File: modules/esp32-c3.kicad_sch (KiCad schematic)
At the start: 20 parts, among them U2 ESP32-C3, U3 W25X40CLSN, Y1 40MHz

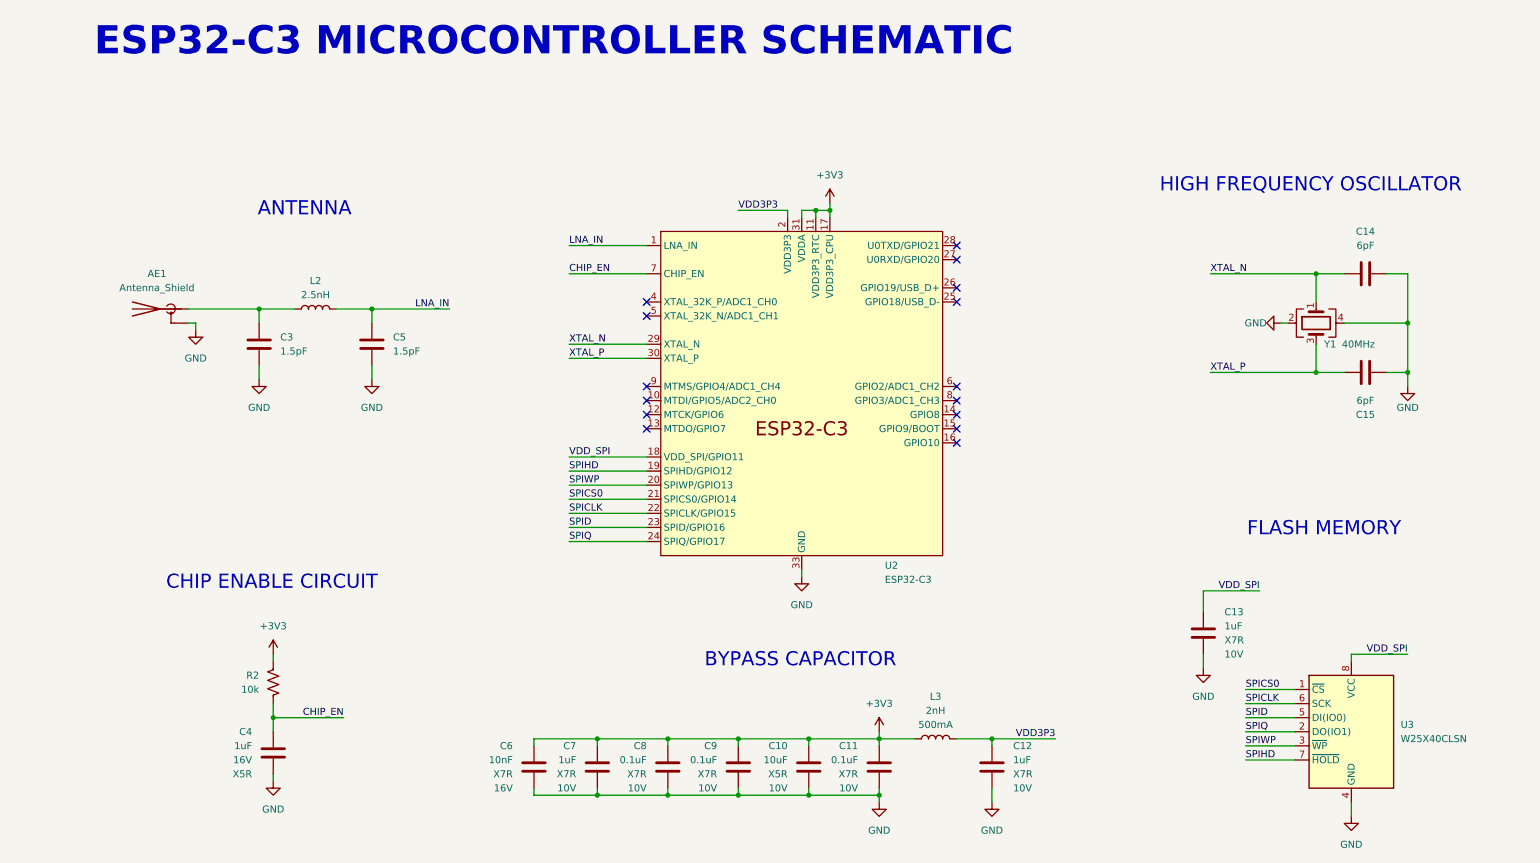
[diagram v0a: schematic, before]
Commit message: Made the first version of the layout with the ESP32-C3
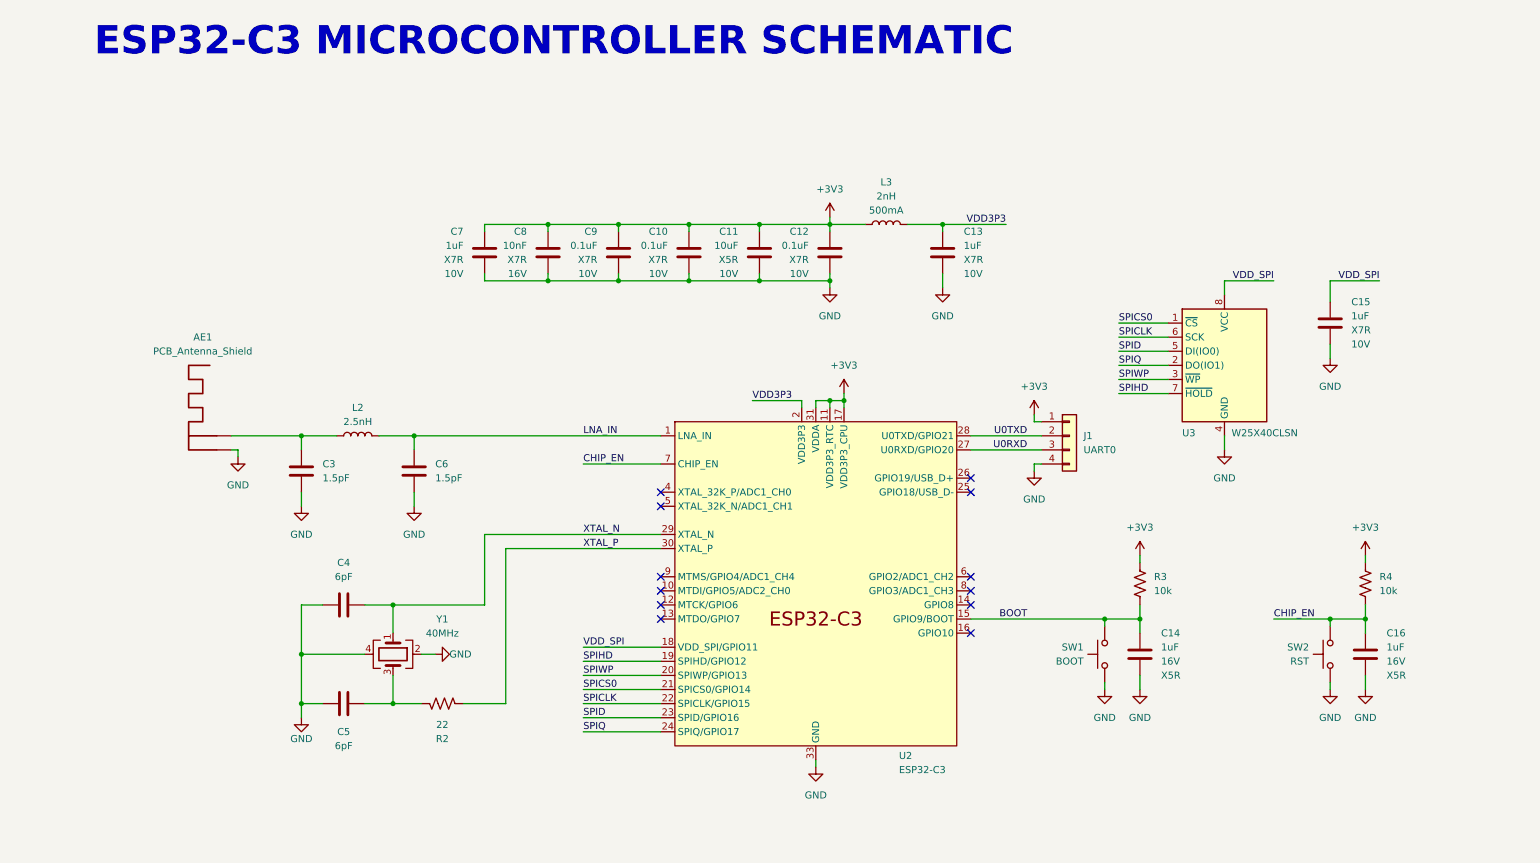
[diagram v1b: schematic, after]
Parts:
- removed AE1: Antenna_Shield, symbol Device:Antenna_Shield
- added AE1: PCB_Antenna_Shield, RF_Antenna:PCB_ANTENNA_2,4GHz_50Ohm, symbol Device:PCB_Antenna_Shield
- added C14: 1uF, Capacitor_SMD:C_0603_1608Metric, symbol Device:C
- added J1: UART0, Connector_PinHeader_2.00mm:PinHeader_1x04_P2.00mm_Vertical, symbol Connector_Generic:Conn_01x04
- added R2: 22, Resistor_SMD:R_0603_1608Metric, symbol Device:R_US
- added R3: 10k, Resistor_SMD:R_0603_1608Metric, symbol Device:R_US
- added SW1: BOOT, Button_Switch_THT:SW_PUSH_1P1T_6x3.5mm_H5.0_APEM_MJTP1250, symbol Switch:SW_Push
- added SW2: RST, Button_Switch_THT:SW_PUSH_1P1T_6x3.5mm_H5.0_APEM_MJTP1250, symbol Switch:SW_Push
- renumbered C9 to C10, C10 to C11, C11 to C12, C12 to C13, C13 to C15, C4 to C16, C14 to C4, C15 to C5, C5 to C6, C6 to C8, C8 to C9, R2 to R4
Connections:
- net +3V3: now also J1.1 (Pin_1), R3.1
- net CHIP_EN: now also SW2.2
- net GND: now also AE1.2 (Shield), C14.2, J1.4 (Pin_4), SW1.1, SW2.1
- net XTAL_P: now also R2.2; no longer C5.2, Y1.3
- net BOOT: now reaches U2.15 (GPIO9/BOOT)
- net BOOT: now also C14.1, R3.2, SW1.2
- net U0RXD: now reaches U2.27 (U0RXD/GPIO20)
- net U0RXD: now also J1.3 (Pin_3)
- net U0TXD: now reaches U2.28 (U0TXD/GPIO21)
- net U0TXD: now also J1.2 (Pin_2)
- net at C3.1, L2.1: now also AE1.1 (A)
- new net: C5.2, R2.1, Y1.3
- no-connect marks 15 -> 12
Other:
- note removed: "ANTENNA"
- note removed: "BYPASS CAPACITOR"
- note removed: "CHIP ENABLE CIRCUIT"
- note removed: "FLASH MEMORY"
- note removed: "HIGH FREQUENCY OSCILLATOR"
- moved on the sheet: C10, C11, C12, C13, C15, C16, C3, C4, C5, C6, C7, C8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

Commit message: Made some fixes with the layout
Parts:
- C11: footprint Capacitor_SMD:C_0805_2012Metric -> Capacitor_SMD:C_0402_1005Metric; Descrip CAP CER 10UF 10V X5R 0805 -> CAP CER 10UF 10V X5R 0402; Manufacturer Samsung Electro-Mechanics -> Murata Electronics; Mfg Part # CL21A106KPFNNNE -> GRM155R61A106ME11D; Price 0,02060 -> 0,01680; Tol (none) -> ±20%
- C13, C15, C7: footprint Capacitor_SMD:C_0603_1608Metric -> Capacitor_SMD:C_0402_1005Metric; Descrip CAP CER 1UF 10V X7R 0603 -> CAP CER 1UF 10V X7R 0402; Manufacturer Samsung Electro-Mechanics -> Murata Electronics; Mfg Part # CL10B105KP8NNNC -> GRM155Z71A105KE01D; Price 0,00800 -> 0,01280
- C14, C16: footprint Capacitor_SMD:C_0603_1608Metric -> Capacitor_SMD:C_0402_1005Metric; Descrip CAP CER 1UF 16V X5R 0603 -> CAP CER 1UF 10V X7R 0402; Manufacturer Samsung Electro-Mechanics -> Murata Electronics; Mfg Part # CL10A105KO8NNNC -> GRM155Z71A105KE01D; Price 0,00720 -> 0,01280; TC X5R -> X7R; Tol ±10% -> (none); VOLTAGE 16V -> 10V
- C4, C5: footprint Capacitor_SMD:C_0603_1608Metric -> Capacitor_SMD:C_0402_1005Metric; Descrip CAP CER 6PF 50V C0G/NP0 0603 -> CAP CER 6PF 50V C0G/NPO 0402; Manufacturer Walsin Technology Corporation -> YAGEO; Mfg Part # 0603N6R0D500CT -> CC0402BRNPO9BN6R0; Price 0,00738 -> 0,00839; Tol ±0.5pF -> ±0.1pF
- C8: footprint Capacitor_SMD:C_0603_1608Metric -> Capacitor_SMD:C_0402_1005Metric; Descrip CAP CER 10NF 16V X7R 0603 -> CAP CER 0402 10NF 25V X7R 10%; Manufacturer Samsung Electro-Mechanics -> KEMET; Mfg Part # CL10B103KO8WPNC -> C0402C103K3REC7411; Price 0,01485 -> 0,01989; VOLTAGE 16V -> 25V
- R2: footprint Resistor_SMD:R_0603_1608Metric -> Resistor_SMD:R_0402_1005Metric; Descrip RES 22 OHM 1% 1/10W 0603 -> RES SMD 22 OHM 1% 1/10W 0402; Manufacturer YAGEO -> Panasonic Electronic Components; Mfg Part # RC0603FR-0722RL -> ERJ-2RKF22R0X; Price 0,00408 -> 0,00720
- R3, R4: footprint Resistor_SMD:R_0603_1608Metric -> Resistor_SMD:R_0402_1005Metric; Descrip RES 10K OHM 1% 1/10W 0603 -> RES SMD 10K OHM 1% 1/10W 0402; Manufacturer YAGEO -> Panasonic Electronic Components; Mfg Part # RC0603FR-0710KL -> ERJ-2RKF1002X; Price 0,00612 -> 0,00720
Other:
- moved on the sheet: AE1, C3, C6, L2

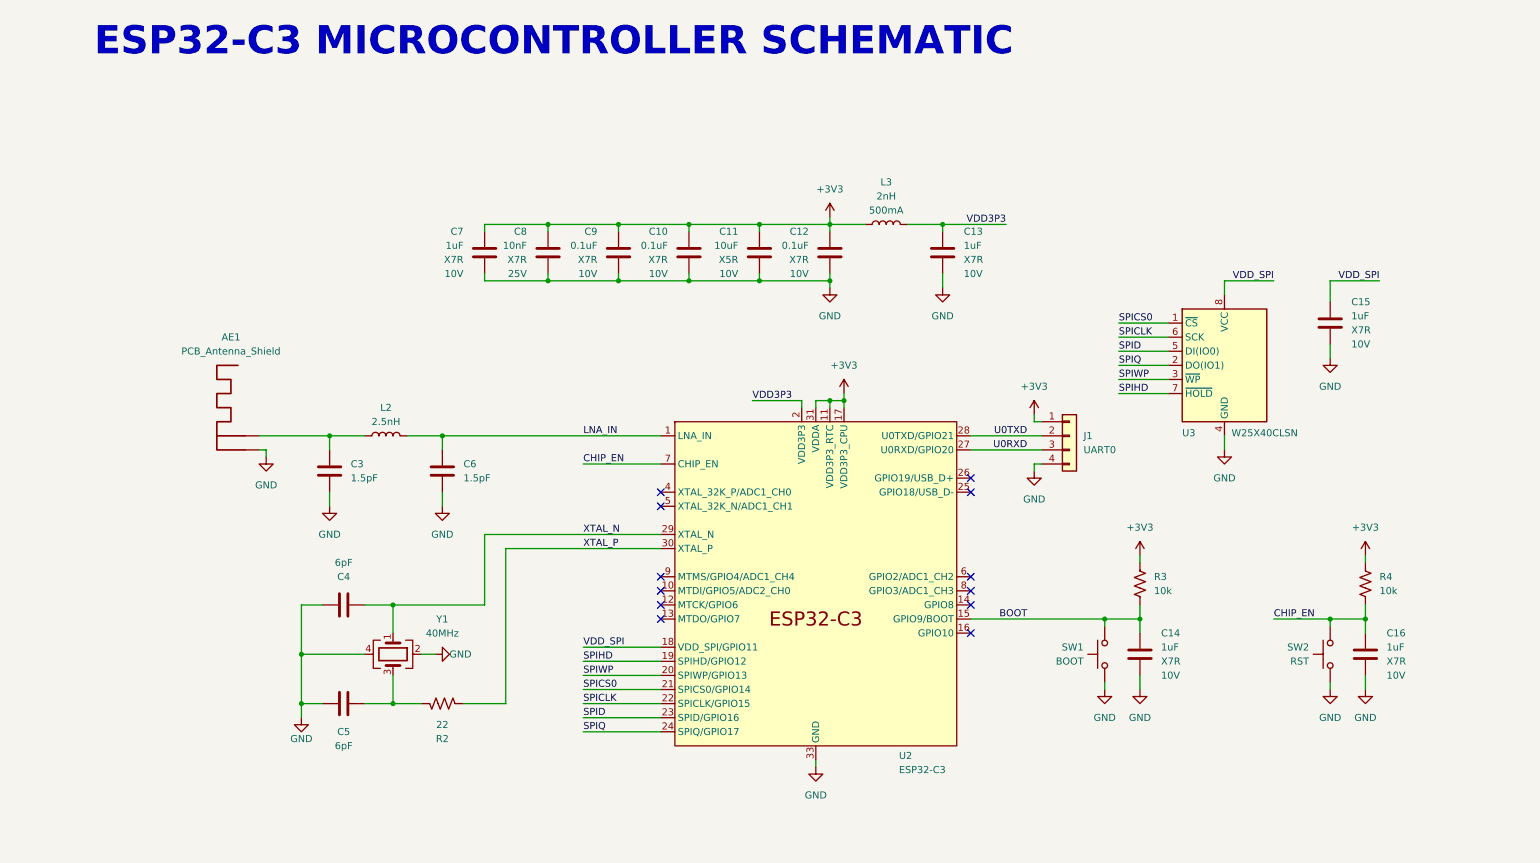
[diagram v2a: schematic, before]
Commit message: Made the first version of the layout - DRC OK
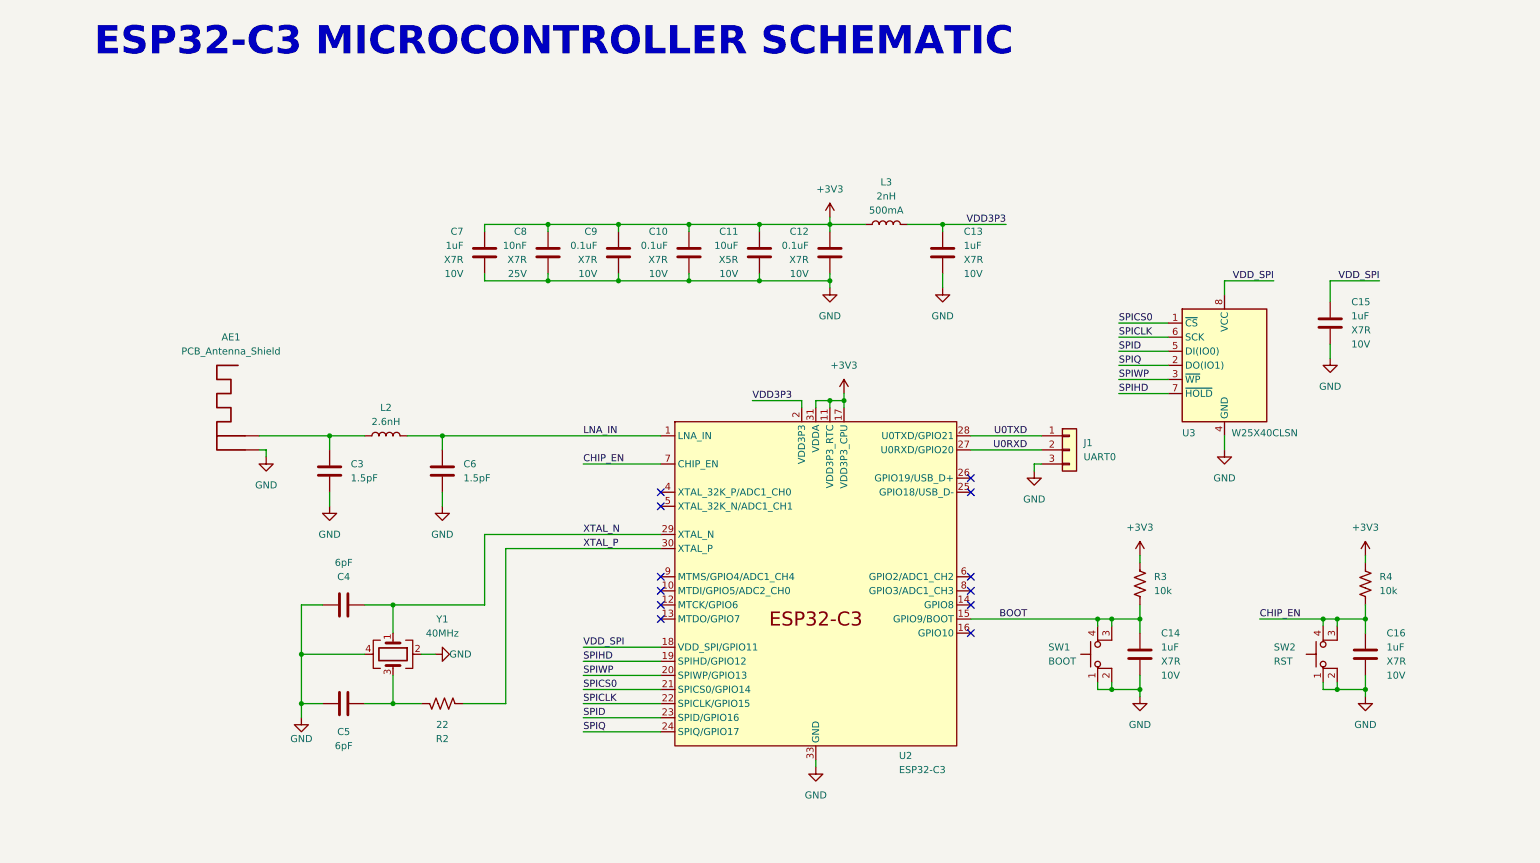
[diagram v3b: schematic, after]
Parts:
- removed SW1: BOOT, Button_Switch_THT:SW_PUSH_1P1T_6x3.5mm_H5.0_APEM_MJTP1250, symbol Switch:SW_Push
- removed SW2: RST, Button_Switch_THT:SW_PUSH_1P1T_6x3.5mm_H5.0_APEM_MJTP1250, symbol Switch:SW_Push
- added SW1: BOOT, MSS_Devices:SW_SPST_PTS815, symbol Switch:SW_MEC_5E
- added SW2: RST, MSS_Devices:SW_SPST_PTS815, symbol Switch:SW_MEC_5E
- C3, C6: Descrip CAP CER 1.5PF 25V C0G/NP0 0201 -> CAP CER 1.5PF 50V C0G/NP0 0201; Mfg Part # GRM0335C1E1R5BA01D -> GRM0335C1H1R5BA01D; Price 0,00578 -> 0,00398; VOLTAGE 25V -> 50V
- J1: footprint Connector_PinHeader_2.00mm:PinHeader_1x04_P2.00mm_Vertical -> Connector_PinHeader_2.00mm:PinHeader_1x03_P2.00mm_Vertical; symbol Connector_Generic:Conn_01x04 -> Connector_Generic:Conn_01x03
- L2: value 2.5nH -> 2.6nH; Descrip FIXED IND 2.5NH 500MA 200MOHM SM -> FIXED IND 2.6NH 500MA 200MOHM SM; Mfg Part # LQP03TN2N5B02D -> LQP03TN2N6B02D
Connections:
- net +3V3: no longer J1.1 (Pin_1)
- net BOOT: now also SW1.3 (K), SW1.4 (A)
- net CHIP_EN: now also SW2.3 (K), SW2.4 (A)
- net GND: now also J1.3 (Pin_3), SW1.1, SW1.2, SW2.1, SW2.2; no longer J1.4 (Pin_4)
- net U0RXD: now also J1.2 (Pin_2); no longer J1.3 (Pin_3)
- net U0TXD: now also J1.1 (Pin_1); no longer J1.2 (Pin_2)

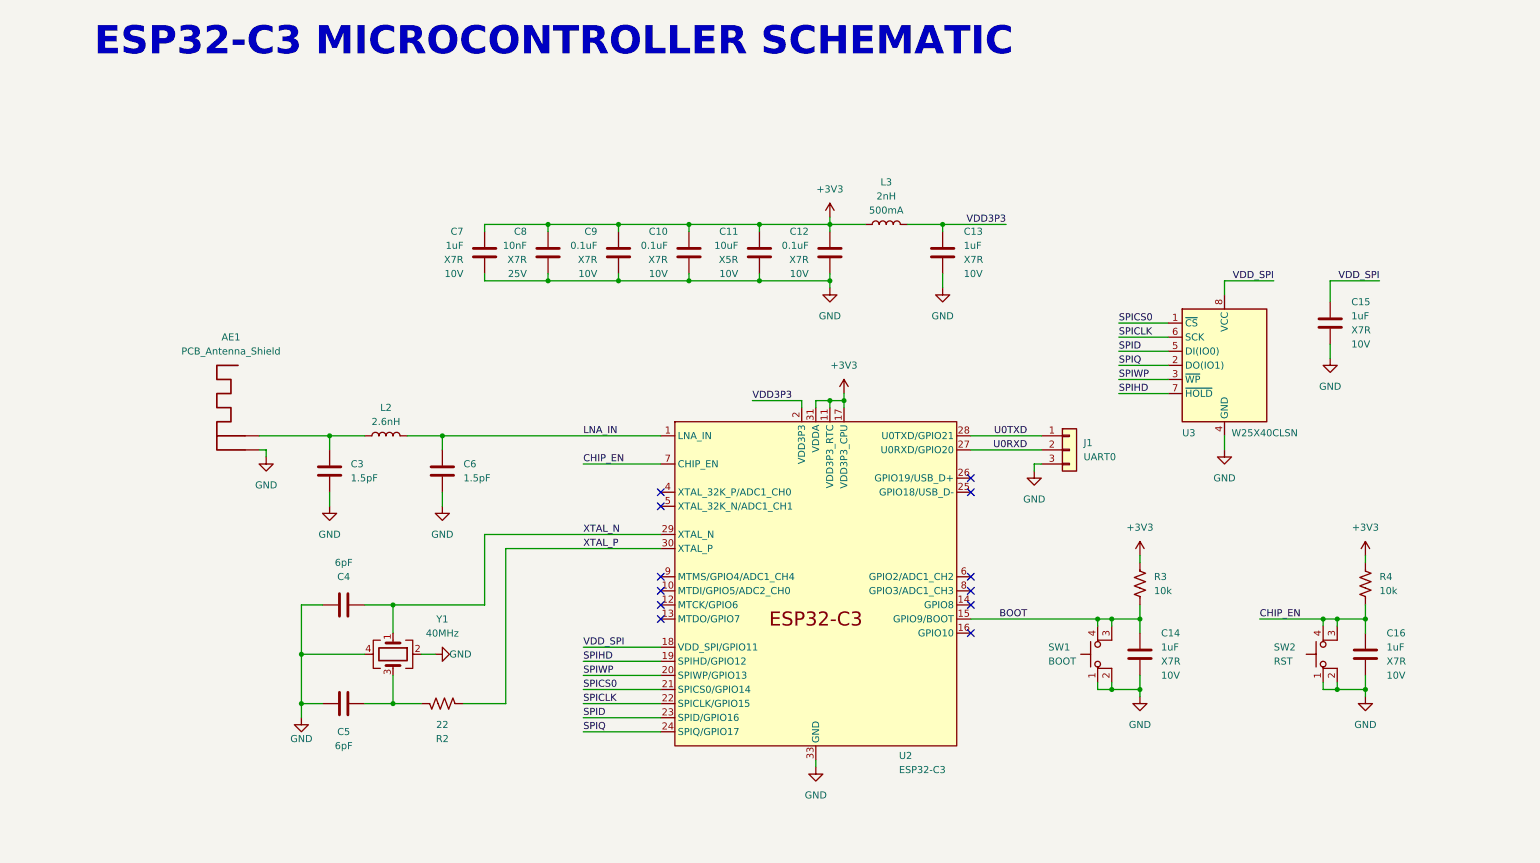
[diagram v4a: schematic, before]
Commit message: Solved some warnings
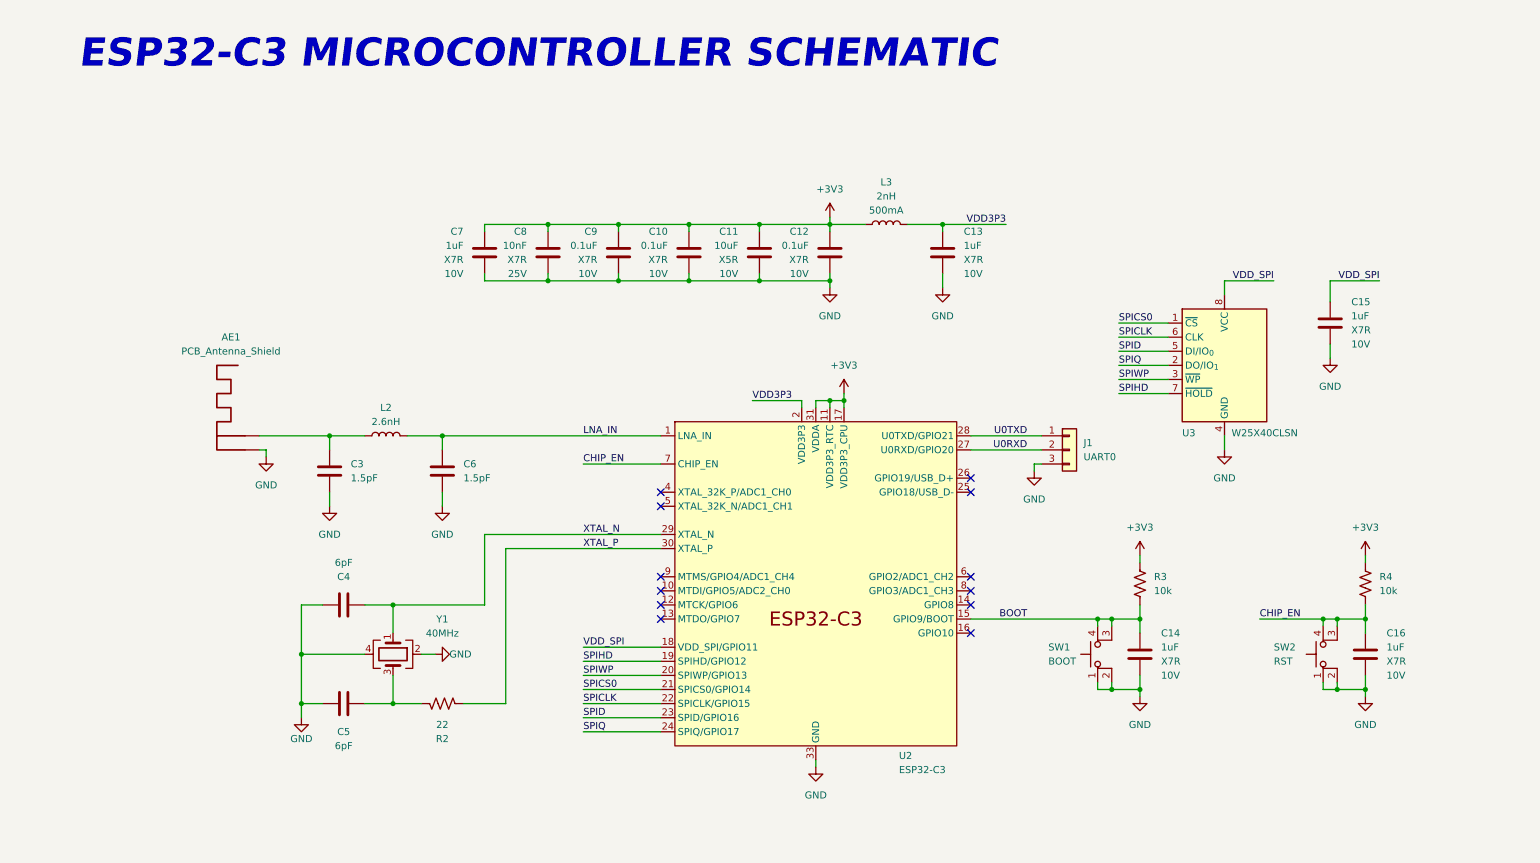
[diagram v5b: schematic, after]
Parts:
- AE1: footprint RF_Antenna:PCB_ANTENNA_2,4GHz_50Ohm -> RF_Antenna:Texas_SWRA117D_2.4GHz_Left
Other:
- title: (none) -> ${TITLE}
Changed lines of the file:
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@@
 	(paper "A4")
 	(title_block
+		(title "${TITLE}")
 		(date "2024-12-11")
 		(rev "${VERSION}")
@@
 	(text "ESP32-C3 MICROCONTROLLER SCHEMATIC"
 		(exclude_from_sim no)
-		(at 21.082 24.638 0)
+		(at 101.092 23.876 0)
 		(effects
 			(font
@@
 				(thickness 1.016)
 				(bold yes)
+				(italic yes)
 			)
-			(justify left bottom)
 		)
 	)
@@
 			)
 		)
-		(property "Description" "4Mbit Serial Flash memory, dual I/O SPI, SOIC-8"
+		(property "Description" "4Mbit / 512KiB Serial Flash memory, Standard/Dual I/O SPI, 2.3-3.6V, SOIC-8 (150 mil)"
 			(at 224.79 80.01 0)
 			(effects
@@
 			)
 		)
-		(property "Footprint" "RF_Antenna:PCB_ANTENNA_2,4GHz_50Ohm"
+		(property "Footprint" "RF_Antenna:Texas_SWRA117D_2.4GHz_Left"
 			(at 45.72 92.71 0)
 			(effects
